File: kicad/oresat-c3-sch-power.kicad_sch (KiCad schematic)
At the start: 58 parts, among them U31 LP2985AIM5-3.3, U34 TPS259621DDA, U35 TPS259620DDA, U36 LTC3624-5, U38 LP2985AIM5-3.3, U6 LTC3624-5

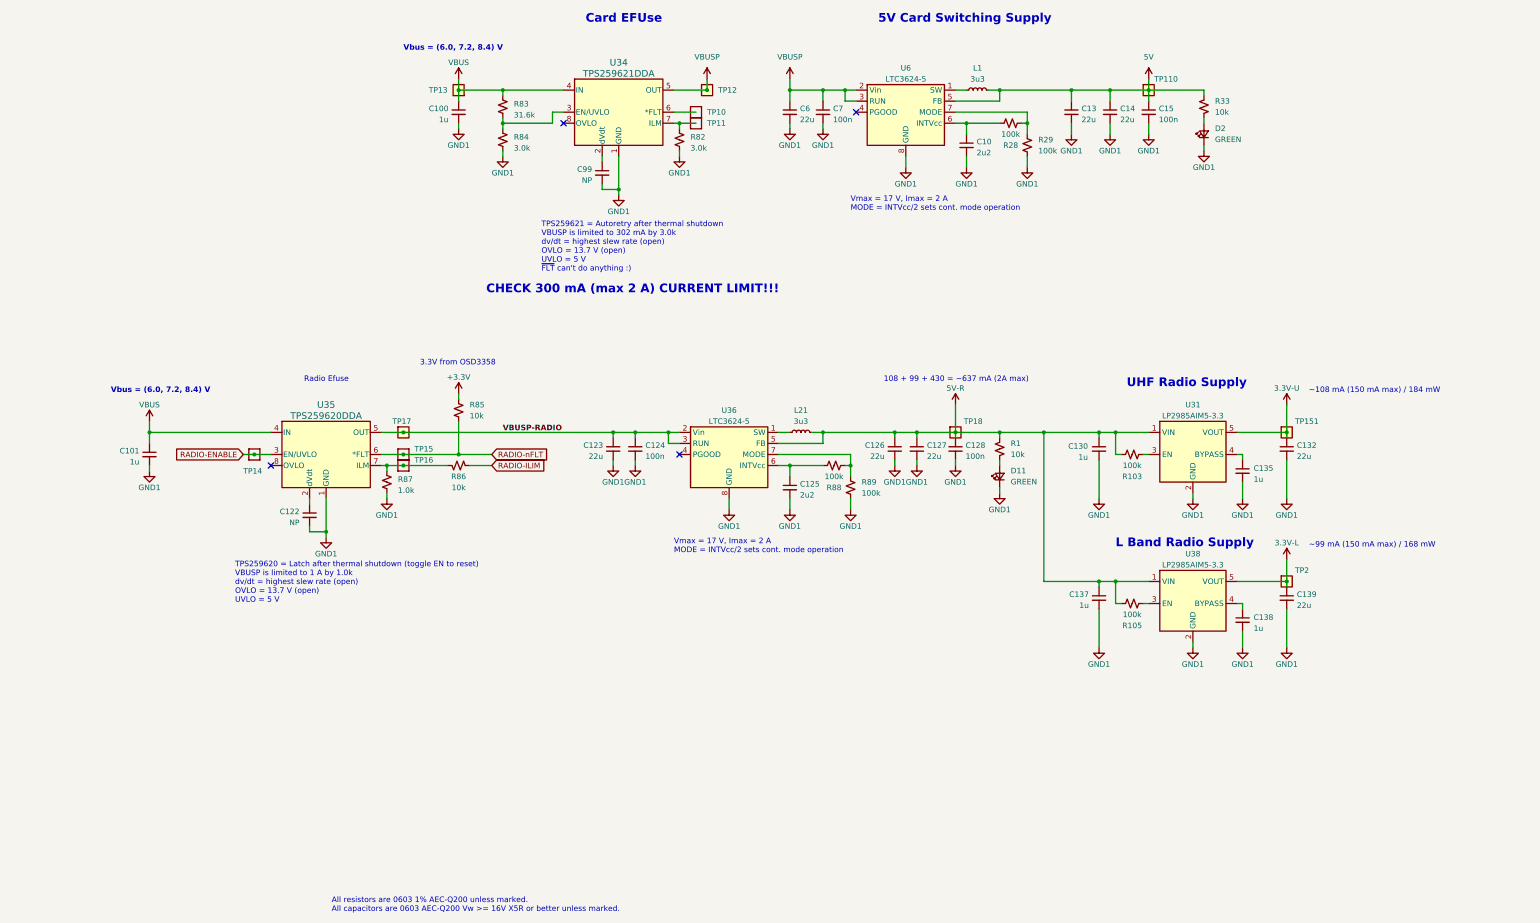
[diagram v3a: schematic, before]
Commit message: Switched all grounds to a single ground, because I can't find a way to overlap ground planes in KiCAD. That's actually not terrible, however, because KiCAD has an anti-plane feature which I used to cut the ground plane between UHF and L radios and L radio and Octavo. So actually I think it came out better than having separate ground planes. Only thing left now are the ~ 40 connections to the Octavo.
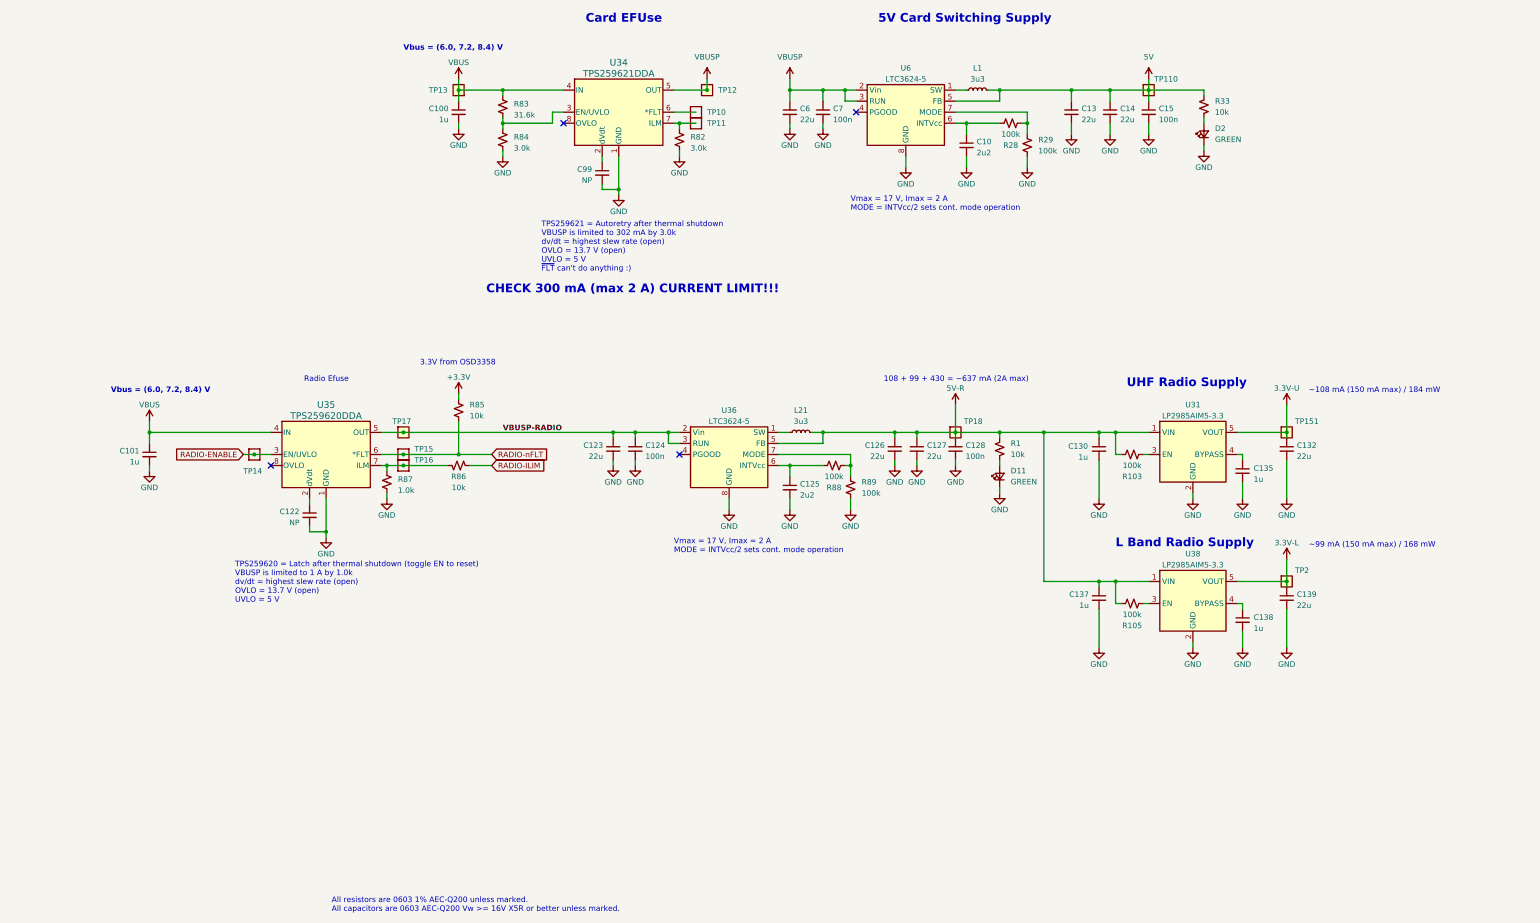
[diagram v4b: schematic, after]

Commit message: Zero airwires! Rough draft schematic and layout are done. Still need ERC and DRC and full design review and stiching and polish.
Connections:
- net +3.3V renamed 3.3V
- net RADIO-ENABLE renamed RADIO_ENABLE
- net RADIO-ILIM renamed RADIO_ILIM
- net RADIO-nFLT renamed RADIO_nFLT

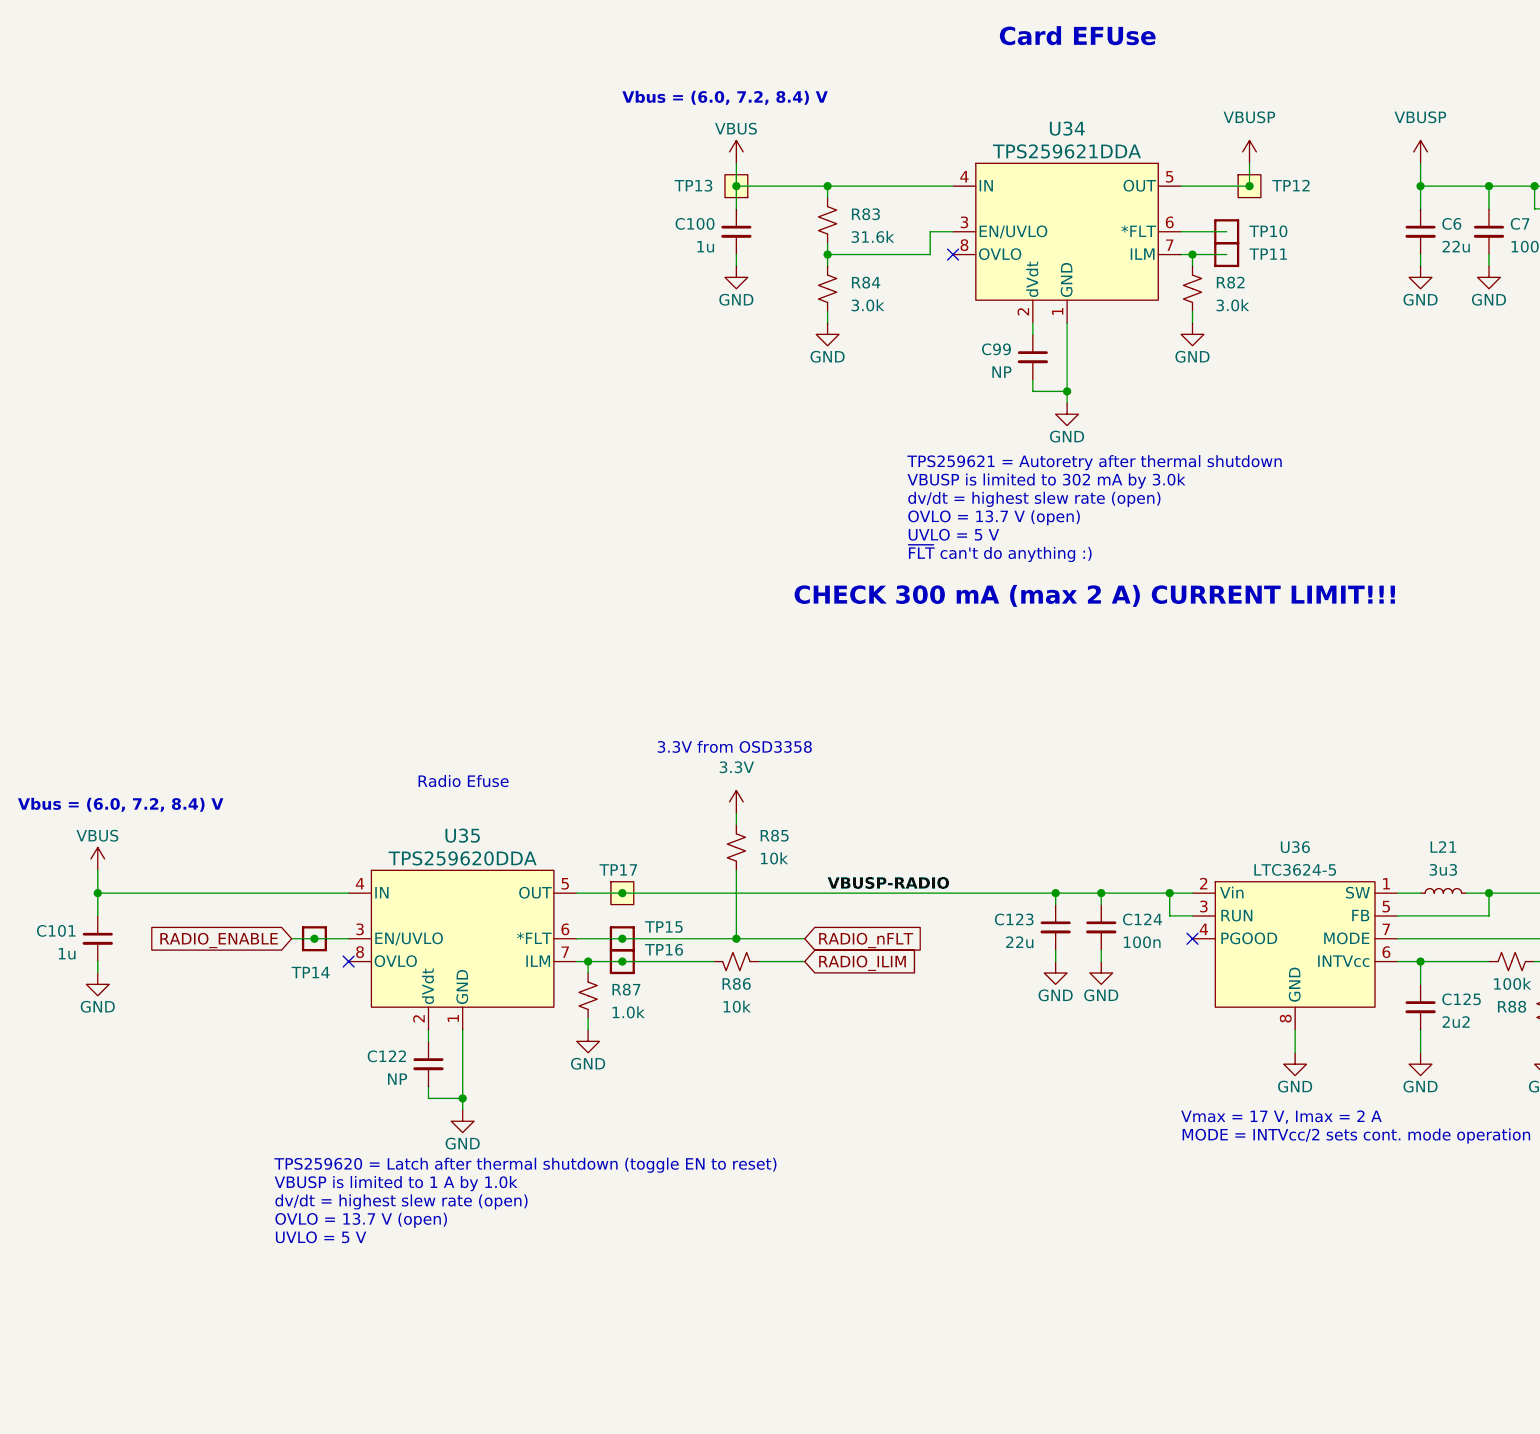
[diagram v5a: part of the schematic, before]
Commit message: An evening of cleanups from the design review. Includes lots of ERC and DRC cleanup, although still over 450 DRC errors mostly from RF keepouts. Fixed PA ground connection, notes on pin reset configuration, and lots of small naggy things. Also cleaned up wierd broken traces on eMMC traces. No longer all same length (sorry Oliver) but it shouldn't affect performance.
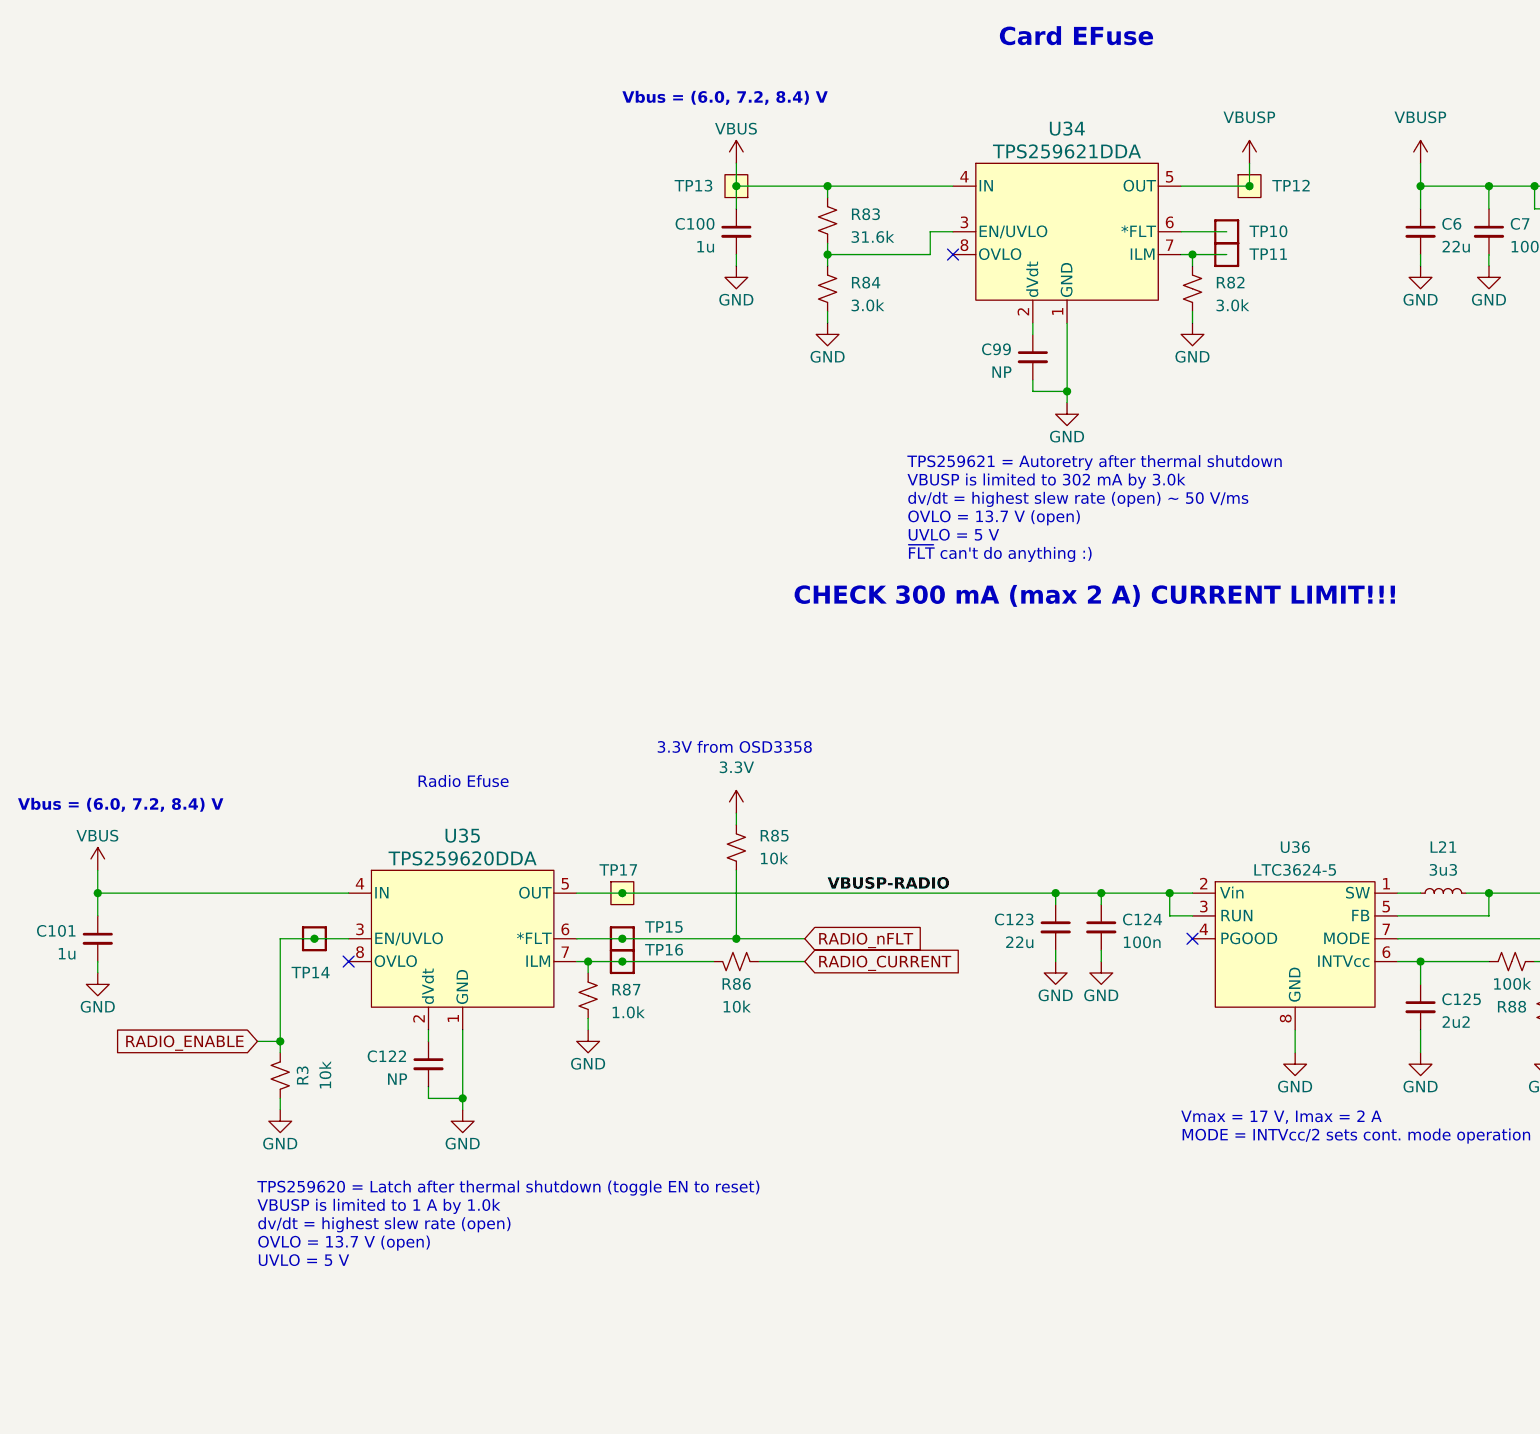
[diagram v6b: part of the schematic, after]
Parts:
- added R3: 10k, Resistor_SMD:R_0603_1608Metric, symbol Device:R_Small_US
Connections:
- net GND: now also R3.2
- net RADIO_ENABLE: now also R3.1
- net RADIO_ILIM renamed RADIO_CURRENT
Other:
- note added: "Card EFuse"
- note added: "TPS259621 = Autoretry after thermal shutdown VBUSP is limited to 302 mA by 3.0k dv/dt = highest slew rate (open) ~ 50 V/ms OVLO = 13.7 V (open) UVLO = 5 V ~{FLT} can't do anything :)"
- note removed: "Card EFUse"
- note removed: "TPS259621 = Autoretry after thermal shutdown VBUSP is limited to 302 mA by 3.0k dv/dt = highest slew rate (open) OVLO = 13.7 V (open) UVLO = 5 V ~{FLT} can't do anything :)"
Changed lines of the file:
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@@
   (junction (at 306.07 72.39) (diameter 0) (color 0 0 0 0)
   )
+  (junction (at 96.52 167.64) (diameter 0) (color 0 0 0 0)
+  )
   (junction (at 223.52 158.75) (diameter 0) (color 0 0 0 0)
   )
@@
     (stroke (width 0) (type default))
   )
+  (wire (pts (xy 96.52 167.64) (xy 93.98 167.64))
+    (stroke (width 0) (type default))
+  )
   (wire (pts (xy 113.03 172.72) (xy 113.03 173.99))
     (stroke (width 0) (type default))
@@
     (stroke (width 0) (type default))
   )
+  (wire (pts (xy 96.52 156.21) (xy 100.33 156.21))
+    (stroke (width 0) (type default))
+  )
   (wire (pts (xy 195.58 151.13) (xy 195.58 153.67))
     (stroke (width 0) (type default))
@@
     (stroke (width 0) (type default))
   )
+  (wire (pts (xy 96.52 173.99) (xy 96.52 175.26))
+    (stroke (width 0) (type default))
+  )
   (wire (pts (xy 157.48 86.36) (xy 157.48 87.63))
     (stroke (width 0) (type default))
@@
     (stroke (width 0) (type default))
   )
-  (wire (pts (xy 100.33 156.21) (xy 97.79 156.21))
-    (stroke (width 0) (type default))
-  )
   (wire (pts (xy 187.96 151.13) (xy 195.58 151.13))
     (stroke (width 0) (type default))
@@
     (stroke (width 0) (type default))
   )
+  (wire (pts (xy 96.52 156.21) (xy 96.52 167.64))
+    (stroke (width 0) (type default))
+  )
   (wire (pts (xy 327.66 200.66) (xy 327.66 196.85))
     (stroke (width 0) (type default))
@@
     (stroke (width 0) (type default))
   )
+  (wire (pts (xy 96.52 167.64) (xy 96.52 168.91))
+    (stroke (width 0) (type default))
+  )
   (wire (pts (xy 223.52 158.75) (xy 223.52 161.29))
     (stroke (width 0) (type default))
@@
     (effects (font (size 1.27 1.27)) (justify left bottom))
   )
-  (text "TPS259621 = Autoretry after thermal shutdown\nVBUSP is limited to 302 mA by 3.0k\ndv/dt = highest slew rate (open)\nOVLO = 13.7 V (open)\nUVLO = 5 V\n~{FLT} can't do anything :)"
+  (text "TPS259621 = Autoretry after thermal shutdown\nVBUSP is limited to 302 mA by 3.0k\ndv/dt = highest slew rate (open) ~ 50 V/ms\nOVLO = 13.7 V (open)\nUVLO = 5 V\n~{FLT} can't do anything :)"
     (at 166.37 114.3 0)
     (effects (font (size 1.27 1.27)) (justify left bottom))
@@
     (effects (font (size 1.27 1.27)) (justify left bottom))
   )
-  (text "Card EFUse" (at 176.53 57.15 0)
+  (text "Card EFuse" (at 176.53 57.15 0)
     (effects (font (size 2 2) (thickness 0.4) bold) (justify left bottom))
   )
   (text "TPS259620 = Latch after thermal shutdown (toggle EN to reset)\nVBUSP is limited to 1 A by 1.0k\ndv/dt = highest slew rate (open)\nOVLO = 13.7 V (open)\nUVLO = 5 V"
-    (at 95.885 190.5 0)
+    (at 93.98 193.04 0)
     (effects (font (size 1.27 1.27)) (justify left bottom))
   )
@@
     (effects (font (size 1.27 1.27) bold) (justify left bottom))
   )
-  (global_label "RADIO_ILIM" (shape input) (at 154.94 158.75 0) (fields_autoplaced)
+  (global_label "RADIO_CURRENT" (shape input) (at 154.94 158.75 0) (fields_autoplaced)
     (effects (font (size 1.27 1.27)) (justify left))
-    (property "Intersheetrefs" "${INTERSHEET_REFS}" (at 168.0664 158.75 0)
+    (property "Intersheetrefs" "${INTERSHEET_REFS}" (at 172.9649 158.75 0)
       (effects (font (size 1.27 1.27)) (justify left))
     )
   )
-  (global_label "RADIO_ENABLE" (shape input) (at 97.79 156.21 180) (fields_autoplaced)
+  (global_label "RADIO_ENABLE" (shape input) (at 93.98 167.64 180) (fields_autoplaced)
     (effects (font (size 1.27 1.27)) (justify right))
-    (property "Intersheetrefs" "${INTERSHEET_REFS}" (at 81.3375 156.21 0)
+    (property "Intersheetrefs" "${INTERSHEET_REFS}" (at 77.5275 167.64 0)
       (effects (font (size 1.27 1.27)) (justify right))
     )
@@
     )
   )
+  (symbol (lib_id "power:GND") (at 96.52 175.26 0) (unit 1)
+    (in_bom yes) (on_board yes) (dnp no)
+    (property "Reference" "#PWR02" (at 96.52 181.61 0)
+      (effects (font (size 1.27 1.27)) hide)
+    )
+    (property "Value" "GND" (at 96.52 179.07 0)
+      (effects (font (size 1.27 1.27)))
+    )
+    (property "Footprint" "" (at 96.52 175.26 0)
+      (effects (font (size 1.27 1.27)) hide)
+    )
+    (property "Datasheet" "" (at 96.52 175.26 0)
+      (effects (font (size 1.27 1.27)) hide)
+    )
+    (pin "1")
+    (instances
+      (project "oresat-c3"
+        (path "/65d12cdd-c326-4033-9053-c59fa4e0b25e/2134bb9a-062c-4e32-a41e-d15ce3545372"
+          (reference "#PWR02") (unit 1)
+        )
+      )
+    )
+  )
   (symbol (lib_id "oresat-power:3.3V-U") (at 337.82 144.78 0) (unit 1)
     (in_bom yes) (on_board yes) (dnp no)
@@
         )
       )
+    )
+  )
+  (symbol (lib_id "Device:R_Small_US") (at 96.52 171.45 0) (mirror y) (unit 1)
+    (in_bom yes) (on_board yes) (dnp no)
+    (property "Reference" "R3" (at 99.06 171.45 90)
+      (effects (font (size 1.27 1.27)))
+    )
+    (property "Value" "10k" (at 101.6 171.45 90)
+      (effects (font (size 1.27 1.27)))
+    )
+    (property "Footprint" "Resistor_SMD:R_0603_1608Metric" (at 96.52 171.45 0)
+      (effects (font (size 1.27 1.27)) hide)
+    )
+    (property "Datasheet" "~" (at 96.52 171.45 0)
+      (effects (font (size 1.27 1.27)) hide)
+    )
+    (pin "1")
+    (pin "2")
+    (instances
+      (project "oresat-c3"
+        (path "/65d12cdd-c326-4033-9053-c59fa4e0b25e/2134bb9a-062c-4e32-a41e-d15ce3545372"
+          (reference "R3") (unit 1)
+        )
+      )

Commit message: Last of the ERC and DRC errors! only polishing left.
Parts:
- L1: footprint oresat-footprints:L_ECS-MPI4040 -> oresat-passives:L_ECS-MPI4040
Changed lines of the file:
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@@
       (effects (font (size 1.27 1.27)))
     )
-    (property "Footprint" "oresat-footprints:L_ECS-MPI4040" (at 266.7 72.39 0)
+    (property "Footprint" "oresat-passives:L_ECS-MPI4040" (at 266.7 72.39 0)
       (effects (font (size 1.27 1.27)) hide)
     )
